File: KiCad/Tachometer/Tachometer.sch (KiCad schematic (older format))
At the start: 108 parts, among them J1 PJ301M-12, J2 PJ301M-12, J3 PJ301M-12, J4 PJ301M-12, J5 PJ301M-12, J6 PJ301M-12, J7 PJ301M-12, J8 PJ301M-12, J9 PJ301M-12, Q1 2N3904, Q10 2N3904, Q11 2N3904, Q12 2N3904, Q13 2N3904, Q14 2N3904, Q15 2N3904, Q16 2N3904, Q17 2N3904, Q18 2N3904, Q2 2N3904, Q3 2N3904, Q4 2N3904, Q5 2N3904, Q6 2N3904, Q7 2N3904, Q8 2N3904, Q9 2N3904

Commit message: ..
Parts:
- C1, C10, C11, C12, C13, C14, C15, C16, C17, C18, C2, C3, C4, C5, C6, C7, C8, C9: footprint Capacitor_THT:CP_Axial_L20.0mm_D10.0mm_P26.00mm_Horizontal -> Capacitor_THT:C_Disc_D10.0mm_W2.5mm_P5.00mm
- D10: footprint Diode_THT:D_DO-15_P10.16mm_Horizontal -> Diode_THT:D_A-405_P12.70mm_Horizontal
- D11, D12: footprint Diode_THT:D_DO-35_SOD27_P10.16mm_Horizontal -> Diode_THT:D_A-405_P12.70mm_Horizontal
- Q1, Q10, Q11, Q12, Q13, Q14, Q15, Q16, Q17, Q18, Q2, Q3, Q4, Q5, Q6, Q7, Q8, Q9: footprint Package_TO_SOT_THT:TO-92_Inline -> Package_TO_SOT_THT:TO-92L_HandSolder
- R1, R10, R11, R12, R13, R14, R15, R16, R17, R18, R19, R2, R20, R21, R22, R23, R24, R25, R26, R27, R28, R29, R3, R30, R31, R32, R33, R34, R35, R36, R37, R38, R39, R4, R40, R41, R42, R43, R44, R45, R5, R6, R7, R8, R9: footprint Resistor_THT:R_Axial_DIN0207_L6.3mm_D2.5mm_P10.16mm_Horizontal -> Resistor_THT:R_Axial_DIN0411_L9.9mm_D3.6mm_P7.62mm_Vertical

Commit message: all work
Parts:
- removed FB1, FB2, FB3: Ferrite_Bead_Small, symbol Device:Ferrite_Bead_Small
- C1: renamed from C18; value CP1_Small -> 470n
- C10: renamed from C9; value CP1_Small -> 100n
- C11: renamed from C8; value CP1_Small -> 100n
- C12: renamed from C7; value CP1_Small -> 100n
- C13: renamed from C6; value CP1_Small -> 100n
- C14: renamed from C5; value CP1_Small -> 100n
- C15: renamed from C4; value CP1_Small -> 100n
- C16: renamed from C3; value CP1_Small -> 22u
- C17: renamed from C2; value CP1_Small -> 22u
- C18: renamed from C1; value CP1_Small -> 22u
- C2: renamed from C17; value CP1_Small -> 470n
- C3: renamed from C16; value CP1_Small -> 470n
- C5: renamed from C14; value CP1_Small -> 100n
- C6: renamed from C13; value CP1_Small -> 100n
- C7: renamed from C12; value CP1_Small -> 100n
- C8: renamed from C11; value CP1_Small -> 100n
- C9: renamed from C10; value CP1_Small -> 100n
- renumbered C15 to C4, D6 to D1, D9 to D10, D8 to D11, D7 to D12, D5 to D2, D12 to D3, D11 to D4, D10 to D5, D4 to D6, D3 to D7, D2 to D8, D1 to D9, J6 to J1, J5 to J2, J4 to J3, J3 to J4, J2 to J5, J1 to J6, J9 to J7, J7 to J9, Q6 to Q1, Q8 to Q10, Q1 to Q11, Q7 to Q12, Q15 to Q13, Q18 to Q14, Q14 to Q15, Q17 to Q16, Q13 to Q17, Q16 to Q18, Q12 to Q2, Q5 to Q3, Q11 to Q4, Q4 to Q5, Q10 to Q6, Q3 to Q7, Q9 to Q8, Q2 to Q9, R12 to R1, R17 to R10, R10 to R11, R4 to R12, R22 to R13, R28 to R14, R16 to R15, R9 to R16, R3 to R17, R21 to R18, R27 to R19, R6 to R2, R15 to R20, R8 to R21, R2 to R22, R20 to R23, R26 to R24, R14 to R25, R7 to R26, R1 to R27, R19 to R28, R25 to R29, R24 to R3, R13 to R30, R36 to R31, R33 to R32, R42 to R33, R45 to R34, R39 to R35, R35 to R36, R32 to R37, R41 to R38, R44 to R39, R30 to R4, R38 to R40, R34 to R41, R31 to R42, R40 to R43, R43 to R44, R37 to R45, R18 to R5, R11 to R6, R5 to R7, R23 to R8, R29 to R9
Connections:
- net labels added: 12V, 5V
- net labels removed: +12V, +5V
- wire segments 259 -> 256
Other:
- moved on the sheet: A1, C1, C10, C11, C12, C13, C14, C15, C16, C17, C18, C2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

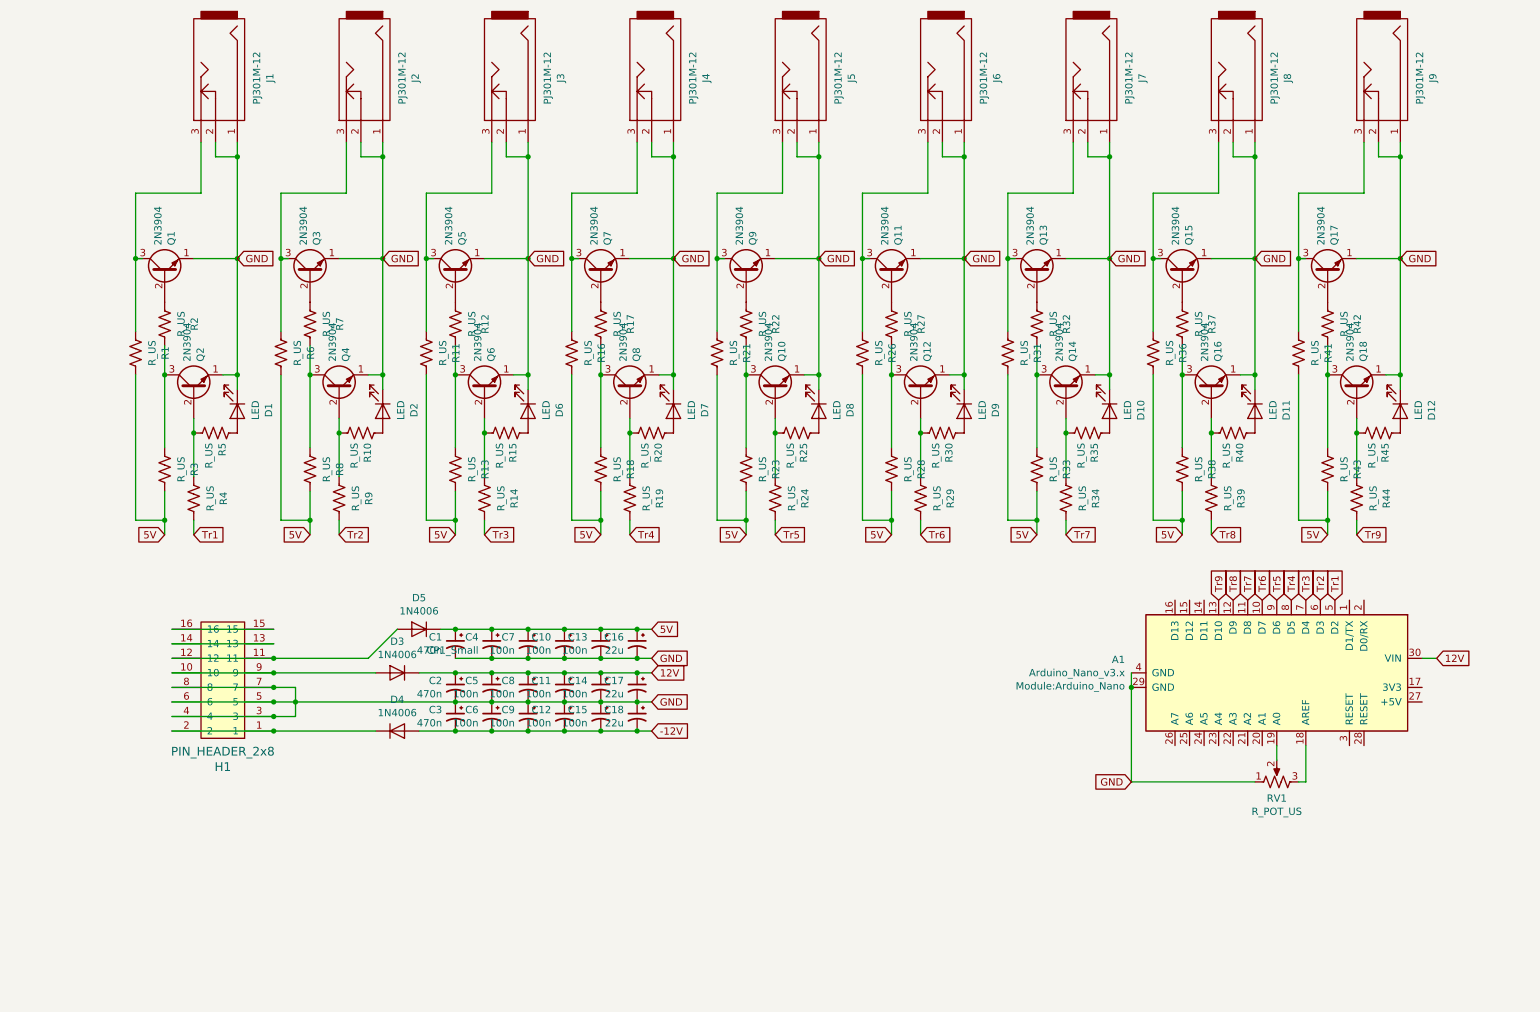
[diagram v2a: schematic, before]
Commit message: added smd footprints
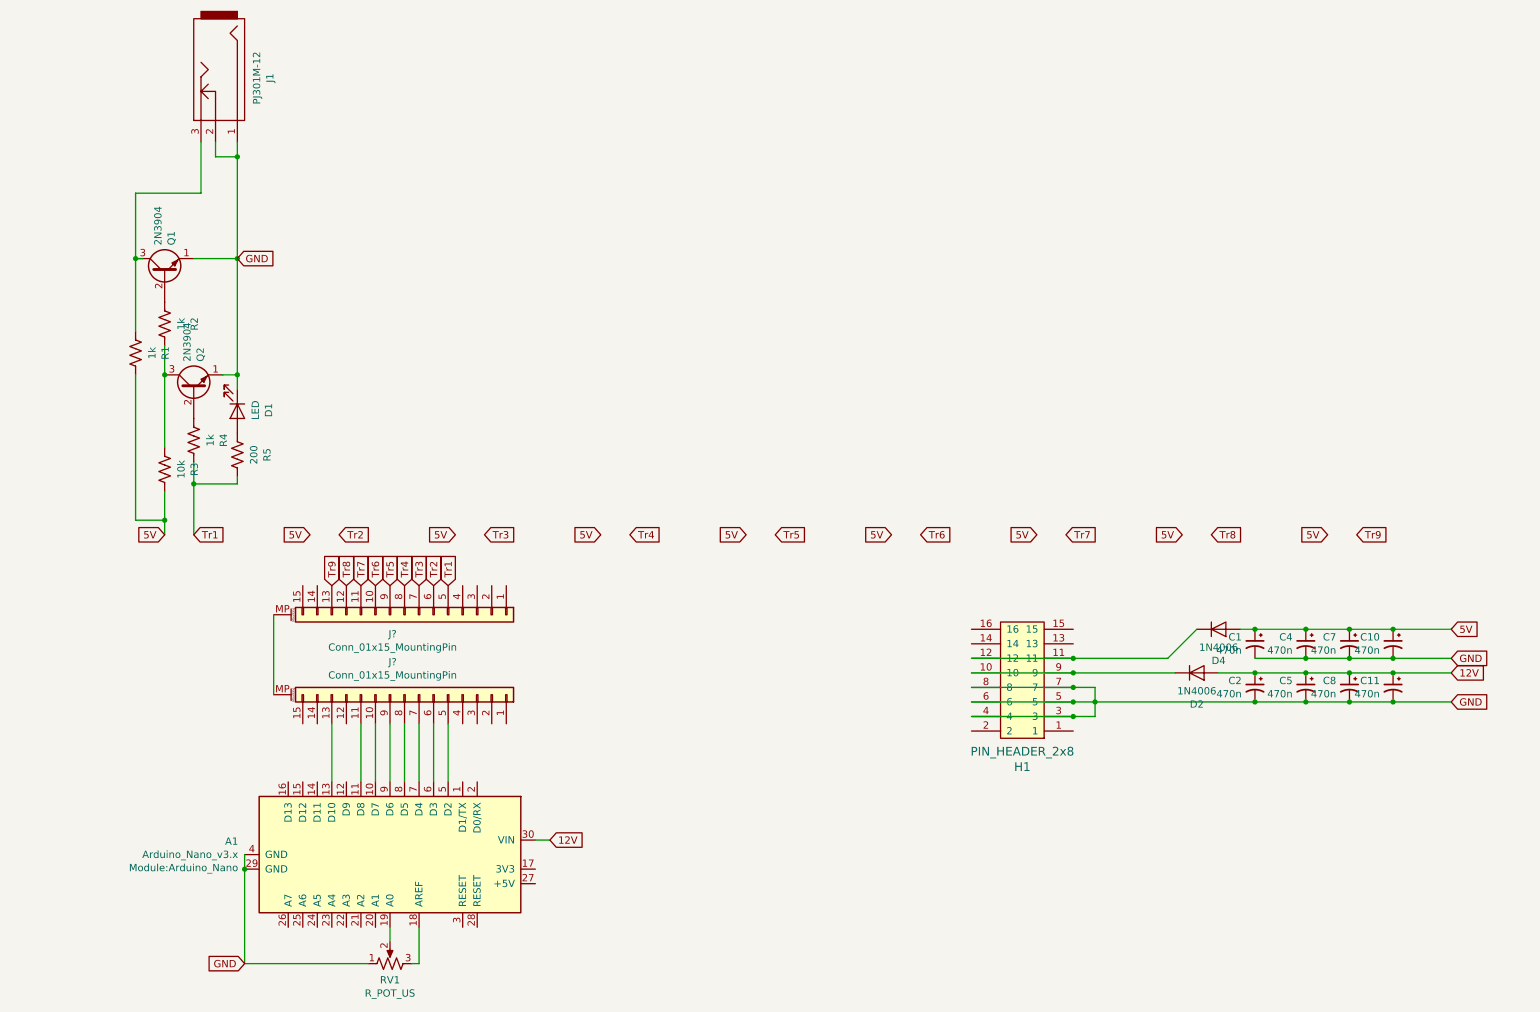
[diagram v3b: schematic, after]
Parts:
- removed C12, C13, C14, C15, C6, C9: 100n, Capacitor_THT:C_Disc_D10.0mm_W2.5mm_P5.00mm, symbol Device:CP1_Small
- removed C16, C17, C18: 22u, Capacitor_THT:C_Disc_D10.0mm_W2.5mm_P5.00mm, symbol Device:CP1_Small
- removed C3: 470n, Capacitor_THT:C_Disc_D10.0mm_W2.5mm_P5.00mm, symbol Device:CP1_Small
- removed D10, D11, D12, D2, D6, D7, D8, D9: LED, LED_THT:LED_D3.0mm_FlatTop, symbol Device:LED
- removed D4: 1N4006, Diode_THT:D_A-405_P12.70mm_Horizontal, symbol Diode:1N4006
- removed J2, J3, J4, J5, J6, J7, J8, J9: PJ301M-12, eurorack:PJ301M-12, symbol Eurorack:PJ301M-12
- removed Q10, Q11, Q12, Q13, Q14, Q15, Q16, Q17, Q18, Q3, Q4, Q5, Q6, Q7, Q8, Q9: 2N3904, Package_TO_SOT_THT:TO-92L_HandSolder, symbol Transistor_BJT:2N3904
- removed R10, R11, R12, R13, R14, R15, R16, R17, R18, R19, R20, R21, R22, R23, R24, R25, R26, R27, R28, R29, R30, R31, R32, R33, R34, R35, R36, R37, R38, R39, R40, R41, R42, R43, R44, R45, R6, R7, R8, R9: R_US, Resistor_THT:R_Axial_DIN0411_L9.9mm_D3.6mm_P7.62mm_Vertical, symbol Device:R_US
- added J? (x2): Conn_01x15_MountingPin, symbol Connector_Generic_MountingPin:Conn_01x15_MountingPin
- C1, C2: footprint Capacitor_THT:C_Disc_D10.0mm_W2.5mm_P5.00mm -> Capacitor_SMD:C_1206_3216Metric_Pad1.42x1.75mm_HandSolder
- C10, C11, C5, C7, C8: value 100n -> 470n; footprint Capacitor_THT:C_Disc_D10.0mm_W2.5mm_P5.00mm -> Capacitor_SMD:C_1206_3216Metric_Pad1.42x1.75mm_HandSolder
- C4: value CP1_Small -> 470n; footprint Capacitor_THT:C_Disc_D10.0mm_W2.5mm_P5.00mm -> Capacitor_SMD:C_1206_3216Metric_Pad1.42x1.75mm_HandSolder
- D2: renamed from D3; footprint Diode_THT:D_A-405_P12.70mm_Horizontal -> Diode_THT:D_DO-41_SOD81_P7.62mm_Horizontal
- D4: renamed from D5; footprint Diode_THT:D_A-405_P12.70mm_Horizontal -> Diode_THT:D_DO-41_SOD81_P7.62mm_Horizontal
- Q1, Q2: footprint Package_TO_SOT_THT:TO-92L_HandSolder -> digikey-footprints:SOT-23-3
- R1, R2, R4: value R_US -> 1k; footprint Resistor_THT:R_Axial_DIN0411_L9.9mm_D3.6mm_P7.62mm_Vertical -> Resistor_SMD:R_1206_3216Metric_Pad1.42x1.75mm_HandSolder
- R3: value R_US -> 10k; footprint Resistor_THT:R_Axial_DIN0411_L9.9mm_D3.6mm_P7.62mm_Vertical -> Resistor_SMD:R_1206_3216Metric_Pad1.42x1.75mm_HandSolder
- R5: value R_US -> 200; footprint Resistor_THT:R_Axial_DIN0411_L9.9mm_D3.6mm_P7.62mm_Vertical -> Resistor_SMD:R_1206_3216Metric_Pad1.42x1.75mm_HandSolder
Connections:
- net labels removed: -12V
- wire segments 256 -> 71
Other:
- moved on the sheet: A1, C1, D2, D4, H1, RV1

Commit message: ruffplaced pcb
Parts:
- removed J? (x2): Conn_01x15_MountingPin, symbol Connector_Generic_MountingPin:Conn_01x15_MountingPin
- added D10, D11, D3, D5, D6, D7, D8, D9: LED, LED_THT:LED_D3.0mm_FlatTop, symbol Device:LED
- added J2, J3, J4, J5, J6, J7, J8, J9: PJ301M-12, eurorack:PJ301M-12, symbol Eurorack:PJ301M-12
- added Q10, Q11, Q12, Q13, Q14, Q15, Q16, Q17, Q18, Q3, Q4, Q5, Q6, Q7, Q8, Q9: 2N3904, digikey-footprints:SOT-23-3, symbol Transistor_BJT:2N3904
- added R10, R15, R20, R25, R30, R35, R40, R45: 200, Resistor_SMD:R_1206_3216Metric_Pad1.42x1.75mm_HandSolder, symbol Device:R_US
- added R11, R12, R14, R16, R17, R19, R21, R22, R24, R26, R27, R29, R31, R32, R34, R36, R37, R39, R41, R42, R44, R6, R7, R9: 1k, Resistor_SMD:R_1206_3216Metric_Pad1.42x1.75mm_HandSolder, symbol Device:R_US
- added R13, R18, R23, R28, R33, R38, R43, R8: 10k, Resistor_SMD:R_1206_3216Metric_Pad1.42x1.75mm_HandSolder, symbol Device:R_US
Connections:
- wire segments 71 -> 246

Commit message: workworkwork
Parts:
- C1: renamed from C11; footprint Capacitor_SMD:C_1206_3216Metric_Pad1.42x1.75mm_HandSolder -> Capacitor_SMD:C_0805_2012Metric_Pad1.15x1.40mm_HandSolder
- C2: renamed from C10; footprint Capacitor_SMD:C_1206_3216Metric_Pad1.42x1.75mm_HandSolder -> Capacitor_SMD:C_0805_2012Metric_Pad1.15x1.40mm_HandSolder
- C3: renamed from C8; footprint Capacitor_SMD:C_1206_3216Metric_Pad1.42x1.75mm_HandSolder -> Capacitor_SMD:C_0805_2012Metric_Pad1.15x1.40mm_HandSolder
- C4: renamed from C7; footprint Capacitor_SMD:C_1206_3216Metric_Pad1.42x1.75mm_HandSolder -> Capacitor_SMD:C_0805_2012Metric_Pad1.15x1.40mm_HandSolder
- C5: footprint Capacitor_SMD:C_1206_3216Metric_Pad1.42x1.75mm_HandSolder -> Capacitor_SMD:C_0805_2012Metric_Pad1.15x1.40mm_HandSolder
- C6: renamed from C4; footprint Capacitor_SMD:C_1206_3216Metric_Pad1.42x1.75mm_HandSolder -> Capacitor_SMD:C_0805_2012Metric_Pad1.15x1.40mm_HandSolder
- C7: renamed from C2; footprint Capacitor_SMD:C_1206_3216Metric_Pad1.42x1.75mm_HandSolder -> Capacitor_SMD:C_0805_2012Metric_Pad1.15x1.40mm_HandSolder
- C8: renamed from C1; footprint Capacitor_SMD:C_1206_3216Metric_Pad1.42x1.75mm_HandSolder -> Capacitor_SMD:C_0805_2012Metric_Pad1.15x1.40mm_HandSolder
- Q1, Q10, Q11, Q12, Q13, Q14, Q15, Q16, Q17, Q18, Q2, Q3, Q4, Q5, Q6, Q7, Q8, Q9: footprint digikey-footprints:SOT-23-3 -> Package_TO_SOT_SMD:SOT-23
- R1, R10, R11, R12, R13, R14, R15, R16, R17, R18, R19, R2, R20, R21, R22, R23, R24, R25, R26, R27, R28, R29, R3, R30, R31, R32, R33, R34, R35, R36, R37, R38, R39, R4, R40, R41, R42, R43, R44, R45, R5, R6, R7, R8, R9: footprint Resistor_SMD:R_1206_3216Metric_Pad1.42x1.75mm_HandSolder -> Resistor_SMD:R_0805_2012Metric_Pad1.15x1.40mm_HandSolder
- RV1: footprint eurorack:Alpha9mmPot -> Potentiometer_THT:Potentiometer_Alpha_RD901F-40-00D_Single_Vertical
- renumbered D2 to D10, D3 to D2, D5 to D3, D6 to D4, D7 to D5, D8 to D6, D9 to D7, D10 to D8, D4 to D9
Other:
- moved on the sheet: A1, C1, C2, C3, C4, C5, C6, C7, C8, D1, D10, D11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
